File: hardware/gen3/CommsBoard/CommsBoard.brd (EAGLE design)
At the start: 140 x 100 mm, 41 parts, among them U1 ATMEGA165PV-8AU

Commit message: hooked up comms to spare header. added breakbeam sensor
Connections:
- new net SPARE1: SPARE_HEADER.1, U1.25
- new net SPARE2: SPARE_HEADER.2, U1.26
- new net SPARE3: SPARE_HEADER.3, U1.27
- new net SPARE4: SPARE_HEADER.4, U1.28
- new net SPARE5: SPARE_HEADER.5, U1.29
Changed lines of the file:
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@@
 <wire x1="81.28" y1="31.115" x2="81" y2="31" width="0.254" layer="1"/>
+</signal>
+<signal name="SPARE1">
+<contactref element="U1" pad="25"/>
+<contactref element="SPARE_HEADER" pad="1"/>
+<wire x1="94" y1="3.127" x2="77.62" y2="68.4064" width="0" layer="19" extent="1-1"/>
+</signal>
+<signal name="SPARE2">
+<contactref element="SPARE_HEADER" pad="2"/>
+<contactref element="U1" pad="26"/>
+<wire x1="96.54" y1="2.873" x2="77.62" y2="69.1938" width="0" layer="19" extent="1-1"/>
+</signal>
+<signal name="SPARE3">
+<contactref element="U1" pad="27"/>
+<contactref element="SPARE_HEADER" pad="3"/>
+<wire x1="99.08" y1="3.127" x2="77.62" y2="70.0066" width="0" layer="19" extent="1-1"/>
+</signal>
+<signal name="SPARE4">
+<contactref element="SPARE_HEADER" pad="4"/>
+<contactref element="U1" pad="28"/>
+<wire x1="101.62" y1="2.873" x2="77.62" y2="70.794" width="0" layer="19" extent="1-1"/>
+</signal>
+<signal name="SPARE5">
+<contactref element="U1" pad="29"/>
+<contactref element="SPARE_HEADER" pad="5"/>
+<wire x1="104.16" y1="3.127" x2="77.62" y2="71.6068" width="0" layer="19" extent="1-1"/>
 </signal>
 </signals>

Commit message: added comments
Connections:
- new net SS_E4: SPI_HEADER.9, U1.56
- new net SS_E5: SPI_HEADER.10, U1.55
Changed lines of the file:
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@@
 <wire x1="104.16" y1="3.127" x2="77.62" y2="71.6068" width="0" layer="19" extent="1-1"/>
+</signal>
+<signal name="SS_E4">
+<contactref element="SPI_HEADER" pad="9"/>
+<contactref element="U1" pad="56"/>
+<wire x1="62.38" y1="68.4064" x2="114.32" y2="97.127" width="0" layer="19" extent="1-1"/>
+</signal>
+<signal name="SS_E5">
+<contactref element="SPI_HEADER" pad="10"/>
+<contactref element="U1" pad="55"/>
+<wire x1="62.38" y1="69.1938" x2="116.86" y2="96.873" width="0" layer="19" extent="1-1"/>
 </signal>
 </signals>

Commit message: some decoupling for power lines
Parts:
- added C5, C6: .1uF, SparkFun-Capacitors:0805
- R2, R3, R4: value 10k -> 4.7k
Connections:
- net 3.3V: now also C6.1
- net 5V: now also C5.1
- net GND: now also C5.2, C6.2
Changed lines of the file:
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@@
 <layers>
 <layer number="1" name="Top" color="4" fill="1" visible="yes" active="yes"/>
+<layer number="2" name="Route2" color="1" fill="3" visible="no" active="no"/>
+<layer number="3" name="Route3" color="4" fill="3" visible="no" active="no"/>
+<layer number="14" name="Route14" color="1" fill="6" visible="no" active="no"/>
+<layer number="15" name="Route15" color="4" fill="6" visible="no" active="no"/>
 <layer number="16" name="Bottom" color="1" fill="1" visible="yes" active="yes"/>
 <layer number="17" name="Pads" color="2" fill="1" visible="yes" active="yes"/>
@@
 <layer number="223" name="223bmp" color="24" fill="1" visible="no" active="no"/>
 <layer number="224" name="224bmp" color="25" fill="1" visible="no" active="no"/>
+<layer number="225" name="225bmp" color="7" fill="1" visible="yes" active="yes"/>
+<layer number="226" name="226bmp" color="7" fill="1" visible="yes" active="yes"/>
+<layer number="227" name="227bmp" color="7" fill="1" visible="yes" active="yes"/>
+<layer number="228" name="228bmp" color="7" fill="1" visible="yes" active="yes"/>
+<layer number="229" name="229bmp" color="7" fill="1" visible="yes" active="yes"/>
+<layer number="230" name="230bmp" color="7" fill="1" visible="yes" active="yes"/>
+<layer number="231" name="231bmp" color="7" fill="1" visible="yes" active="yes"/>
 <layer number="248" name="Housing" color="7" fill="1" visible="yes" active="yes"/>
 <layer number="249" name="Edge" color="7" fill="1" visible="yes" active="yes"/>
@@
 <element name="C2" library="SparkFun-Capacitors" package="0805" value=".1uF" x="56" y="63" rot="R270"/>
 <element name="R1" library="SparkFun-Passives" package="0805" value="10k" x="56" y="59" rot="R270"/>
-<element name="R2" library="SparkFun-Passives" package="0805" value="10k" x="94" y="92" rot="R90"/>
-<element name="R3" library="SparkFun-Passives" package="0805" value="10k" x="97" y="88" rot="R90"/>
-<element name="R4" library="SparkFun-Passives" package="0805" value="10k" x="100" y="92" rot="R90"/>
+<element name="R2" library="SparkFun-Passives" package="0805" value="4.7k" x="94" y="92" rot="R90"/>
+<element name="R3" library="SparkFun-Passives" package="0805" value="4.7k" x="97" y="88" rot="R90"/>
+<element name="R4" library="SparkFun-Passives" package="0805" value="4.7k" x="100" y="92" rot="R90"/>
 <element name="FRAME2" library="SparkFun-Aesthetics" package="CREATIVE_COMMONS" value="FRAME-LETTER" x="88.95" y="-14.47"/>
 <element name="ROBID" library="SparkFun-Electromechanical" package="4-POS-DIP-SMD" value="4-POS-DIP" x="10" y="43" rot="R270">
@@
 </element>
 <element name="JP1" library="SparkFun-Connectors" package="AVR_ICSP" value="M05X2PTH" x="71" y="5" rot="R90"/>
+<element name="C5" library="SparkFun-Capacitors" package="0805" value=".1uF" x="-2" y="-27"/>
+<element name="C6" library="SparkFun-Capacitors" package="0805" value=".1uF" x="-5" y="-27"/>
 </elements>
 <signals>
@@
 <vertex x="1" y="79.4"/>
 </polygon>
+<contactref element="C6" pad="2"/>
+<contactref element="C5" pad="2"/>
+<wire x1="-1.1" y1="-27" x2="59.055" y2="15.5575" width="0" layer="19" extent="1-16"/>
+<wire x1="-4.1" y1="-27" x2="-1.1" y2="-27" width="0" layer="19" extent="1-1"/>
 </signal>
 <signal name="3.3V">
@@
 <wire x1="5.715" y1="73.025" x2="5.555" y2="72.81" width="0.254" layer="1"/>
 <via x="6.985" y="74.295" extent="1-16" drill="0.6096"/>
+<contactref element="C6" pad="1"/>
+<wire x1="-5.9" y1="-27" x2="5.715" y2="39.0525" width="0" layer="19" extent="1-1"/>
 </signal>
 <signal name="FILT">
@@
 <wire x1="33.3375" y1="97.155" x2="33.16" y2="97.127" width="0.254" layer="1"/>
 <wire x1="35.56" y1="97.155" x2="35.7" y2="96.873" width="0.254" layer="1"/>
+<contactref element="C5" pad="1"/>
+<wire x1="-2.9" y1="-27" x2="33.16" y2="97.127" width="0" layer="19" extent="1-1"/>
 </signal>
 <signal name="12VGND">

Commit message: added tmp sensor
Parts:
- added U$2: MCP9700SMD, SparkFun-Sensors:SOT23-3
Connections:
- new net TSENSE: U$2.2, U1.54
- net 3.3V: now also U$2.1
- net GND: now also U$2.3
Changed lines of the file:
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@@
 <element name="C5" library="SparkFun-Capacitors" package="0805" value=".1uF" x="-2" y="-27"/>
 <element name="C6" library="SparkFun-Capacitors" package="0805" value=".1uF" x="-5" y="-27"/>
+<element name="U$2" library="SparkFun-Sensors" package="SOT23-3" value="MCP9700SMD" x="-9" y="-27">
+<attribute name="PROD_ID" value="IC-08917" x="-9" y="-27" size="1.778" layer="27" display="off"/>
+</element>
 </elements>
 <signals>
@@
 <contactref element="C6" pad="2"/>
 <contactref element="C5" pad="2"/>
+<contactref element="U$2" pad="3"/>
 <wire x1="-1.1" y1="-27" x2="59.055" y2="15.5575" width="0" layer="19" extent="1-16"/>
 <wire x1="-4.1" y1="-27" x2="-1.1" y2="-27" width="0" layer="19" extent="1-1"/>
+<wire x1="-9" y1="-25.9" x2="-4.1" y2="-27" width="0" layer="19" extent="1-1"/>
 </signal>
 <signal name="3.3V">
@@
 <via x="6.985" y="74.295" extent="1-16" drill="0.6096"/>
 <contactref element="C6" pad="1"/>
+<contactref element="U$2" pad="1"/>
 <wire x1="-5.9" y1="-27" x2="5.715" y2="39.0525" width="0" layer="19" extent="1-1"/>
+<wire x1="-9.95" y1="-28" x2="-5.9" y2="-27" width="0" layer="19" extent="1-1"/>
 </signal>
 <signal name="FILT">
@@
 <wire x1="62.38" y1="69.1938" x2="116.86" y2="96.873" width="0" layer="19" extent="1-1"/>
 </signal>
+<signal name="TSENSE">
+<contactref element="U$2" pad="2"/>
+<contactref element="U1" pad="54"/>
+<wire x1="-8.05" y1="-28" x2="62.38" y2="70.0066" width="0" layer="19" extent="1-1"/>
+</signal>
 </signals>

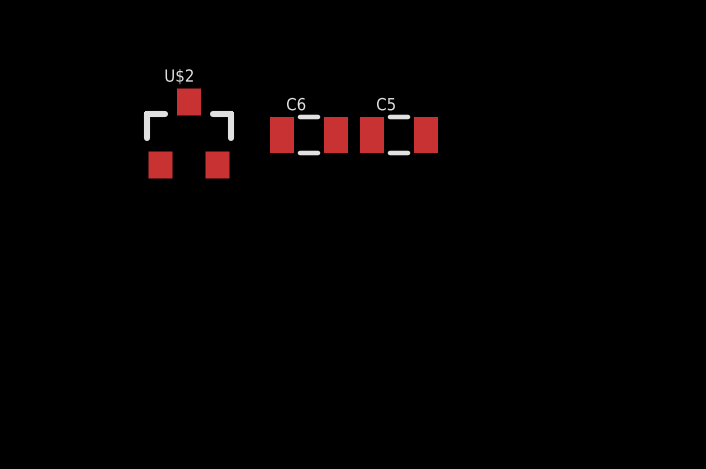
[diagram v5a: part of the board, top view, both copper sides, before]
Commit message: Added reset button to comms
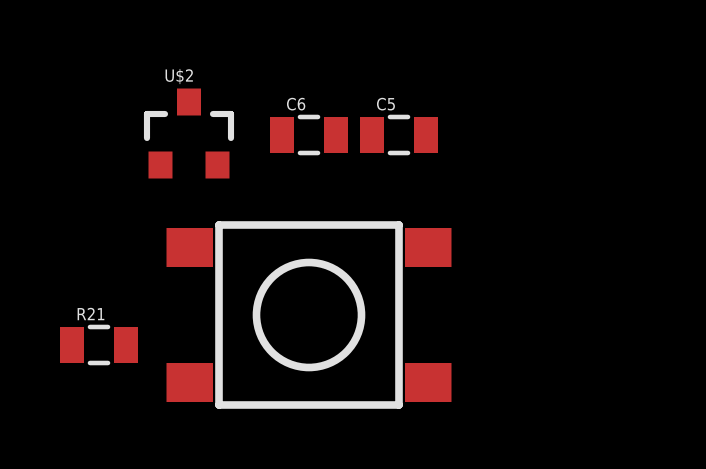
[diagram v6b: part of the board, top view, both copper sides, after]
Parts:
- added R21: 10k, SparkFun-Passives:0805
- added S1: SWITCH-MOMENTARY-2SMD-4, SparkFun-Electromechanical:TACTILE_SWITCH_TALL
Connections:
- net 3.3V: now also R21.2
- net GND: now also S1.B2
- net RESET: now also R21.1, S1.A2
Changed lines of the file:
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@@
 <?xml version="1.0" encoding="utf-8"?>
 <!DOCTYPE eagle SYSTEM "eagle.dtd">
-<eagle version="6.4">
+<eagle version="7.2.0">
 <drawing>
 <settings>
@@
 <pass name="Default">
 <param name="RoutingGrid" value="12.5mil"/>
+<param name="AutoGrid" value="1"/>
+<param name="Efforts" value="0"/>
+<param name="TopRouterVariant" value="1"/>
 <param name="tpViaShape" value="round"/>
 <param name="PrefDir.1" value="*"/>
@@
 <attribute name="PROD_ID" value="IC-08917" x="-9" y="-27" size="1.778" layer="27" display="off"/>
 </element>
+<element name="S1" library="SparkFun-Electromechanical" package="TACTILE_SWITCH_TALL" value="SWITCH-MOMENTARY-2SMD-4" x="-5" y="-33">
+<attribute name="PROD_ID" value="SWCH-11966" x="-5" y="-33" size="1.778" layer="27" display="off"/>
+</element>
+<element name="R21" library="SparkFun-Passives" package="0805" value="10k" x="-12" y="-34"/>
 </elements>
 <signals>
@@
 <contactref element="C5" pad="2"/>
 <contactref element="U$2" pad="3"/>
+<contactref element="S1" pad="B2"/>
 <wire x1="-1.1" y1="-27" x2="59.055" y2="15.5575" width="0" layer="19" extent="1-16"/>
 <wire x1="-4.1" y1="-27" x2="-1.1" y2="-27" width="0" layer="19" extent="1-1"/>
+<wire x1="-1.025" y1="-30.75" x2="-1.1" y2="-27" width="0" layer="19" extent="1-1"/>
 <wire x1="-9" y1="-25.9" x2="-4.1" y2="-27" width="0" layer="19" extent="1-1"/>
 </signal>
@@
 <contactref element="C6" pad="1"/>
 <contactref element="U$2" pad="1"/>
+<contactref element="R21" pad="2"/>
 <wire x1="-5.9" y1="-27" x2="5.715" y2="39.0525" width="0" layer="19" extent="1-1"/>
 <wire x1="-9.95" y1="-28" x2="-5.9" y2="-27" width="0" layer="19" extent="1-1"/>
+<wire x1="-11.1" y1="-34" x2="-9.95" y2="-28" width="0" layer="19" extent="1-1"/>
 </signal>
 <signal name="FILT">
@@
 <wire x1="77.7875" y1="64.4525" x2="77.62" y2="64.3932" width="0.254" layer="1"/>
 <wire x1="71.12" y1="3.4925" x2="71" y2="3.73" width="0.254" layer="1"/>
+<contactref element="S1" pad="A2"/>
+<contactref element="R21" pad="1"/>
+<wire x1="-1.025" y1="-35.25" x2="71.12" y2="3.4925" width="0" layer="19" extent="1-1"/>
+<wire x1="-12.9" y1="-34" x2="-1.025" y2="-35.25" width="0" layer="19" extent="1-1"/>
 </signal>
 <signal name="12V">

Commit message: Added IMU header to comms board
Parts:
- added M5LOCK: IMU_HEADER, SparkFun-Connectors:1X05_LOCK
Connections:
- new net INT: M5LOCK.1, U1.5
- new net SCL: M5LOCK.2, U1.6
- new net SDA: M5LOCK.3, U1.7
- net 3.3V: now also M5LOCK.5
- net CTS: now also U1.9; no longer U1.6
- net GND: now also M5LOCK.4
- net RTS: now also U1.8; no longer U1.5
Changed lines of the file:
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@@
 </element>
 <element name="R21" library="SparkFun-Passives" package="0805" value="10k" x="-12" y="-34"/>
+<element name="M5LOCK" library="SparkFun-Connectors" package="1X05_LOCK" value="IMU_HEADER" x="-11" y="-40"/>
 </elements>
 <signals>
@@
 <contactref element="U$2" pad="3"/>
 <contactref element="S1" pad="B2"/>
+<contactref element="M5LOCK" pad="4"/>
 <wire x1="-1.1" y1="-27" x2="59.055" y2="15.5575" width="0" layer="19" extent="1-16"/>
 <wire x1="-4.1" y1="-27" x2="-1.1" y2="-27" width="0" layer="19" extent="1-1"/>
 <wire x1="-1.025" y1="-30.75" x2="-1.1" y2="-27" width="0" layer="19" extent="1-1"/>
 <wire x1="-9" y1="-25.9" x2="-4.1" y2="-27" width="0" layer="19" extent="1-1"/>
+<wire x1="-3.38" y1="-40.127" x2="-1.025" y2="-30.75" width="0" layer="19" extent="1-1"/>
 </signal>
 <signal name="3.3V">
@@
 <contactref element="U$2" pad="1"/>
 <contactref element="R21" pad="2"/>
+<contactref element="M5LOCK" pad="5"/>
 <wire x1="-5.9" y1="-27" x2="5.715" y2="39.0525" width="0" layer="19" extent="1-1"/>
 <wire x1="-9.95" y1="-28" x2="-5.9" y2="-27" width="0" layer="19" extent="1-1"/>
 <wire x1="-11.1" y1="-34" x2="-9.95" y2="-28" width="0" layer="19" extent="1-1"/>
+<wire x1="-0.84" y1="-39.873" x2="-11.1" y2="-34" width="0" layer="19" extent="1-1"/>
 </signal>
 <signal name="FILT">
@@
 <signal name="RTS">
 <contactref element="U$1" pad="16"/>
-<contactref element="U1" pad="5"/>
 <wire x1="67.31" y1="52.705" x2="67.31" y2="60.325" width="0.254" layer="1"/>
 <wire x1="80.9625" y1="39.0525" x2="67.31" y2="52.705" width="0.254" layer="1"/>
-<wire x1="67.31" y1="60.325" x2="67.206" y2="60.38" width="0.254" layer="1"/>
 <wire x1="80.9625" y1="39.0525" x2="81" y2="39" width="0.254" layer="1"/>
+<contactref element="U1" pad="8"/>
+<wire x1="67.31" y1="60.325" x2="69.5936" y2="60.38" width="0" layer="19" extent="1-1"/>
 </signal>
 <signal name="CTS">
 <contactref element="U$1" pad="12"/>
-<contactref element="U1" pad="6"/>
 <wire x1="67.945" y1="59.69" x2="67.945" y2="60.325" width="0.254" layer="1"/>
 <wire x1="79.375" y1="48.26" x2="67.945" y2="59.69" width="0.254" layer="1"/>
@@
 <wire x1="82.2325" y1="32.0675" x2="82.2325" y2="47.625" width="0.254" layer="1"/>
 <wire x1="81.28" y1="31.115" x2="82.2325" y2="32.0675" width="0.254" layer="1"/>
-<wire x1="67.945" y1="60.325" x2="67.9934" y2="60.38" width="0.254" layer="1"/>
 <wire x1="81.28" y1="31.115" x2="81" y2="31" width="0.254" layer="1"/>
+<contactref element="U1" pad="9"/>
+<wire x1="67.945" y1="60.325" x2="70.4064" y2="60.38" width="0" layer="19" extent="1-1"/>
 </signal>
 <signal name="SPARE1">
@@
 <wire x1="-8.05" y1="-28" x2="62.38" y2="70.0066" width="0" layer="19" extent="1-1"/>
 </signal>
+<signal name="INT">
+<contactref element="U1" pad="5"/>
+<contactref element="M5LOCK" pad="1"/>
+<wire x1="-11" y1="-39.873" x2="67.206" y2="60.38" width="0" layer="19" extent="1-1"/>
+</signal>
+<signal name="SCL">
+<contactref element="U1" pad="6"/>
+<contactref element="M5LOCK" pad="2"/>
+<wire x1="-8.46" y1="-40.127" x2="67.9934" y2="60.38" width="0" layer="19" extent="1-1"/>
+</signal>
+<signal name="SDA">
+<contactref element="U1" pad="7"/>
+<contactref element="M5LOCK" pad="3"/>
+<wire x1="-5.92" y1="-39.873" x2="68.8062" y2="60.38" width="0" layer="19" extent="1-1"/>
+</signal>
 </signals>

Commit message: Added IMU package
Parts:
- removed M5LOCK: IMU_HEADER, SparkFun-Connectors:1X05_LOCK
- added IMU: MPU6050IMUMPU, gen3:MPU-6050IMU
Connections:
- net 3.3V: now also IMU.VCC; no longer M5LOCK.5
- net GND: now also IMU.GND; no longer M5LOCK.4
- net INT: now also IMU.INT; no longer M5LOCK.1
- net SCL: now also IMU.SCL; no longer M5LOCK.2
- net SDA: now also IMU.SDA; no longer M5LOCK.3
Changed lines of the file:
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@@
 </element>
 <element name="R21" library="SparkFun-Passives" package="0805" value="10k" x="-12" y="-34"/>
-<element name="M5LOCK" library="SparkFun-Connectors" package="1X05_LOCK" value="IMU_HEADER" x="-11" y="-40"/>
+<element name="IMU" library="gen3" package="MPU-6050IMU" value="MPU6050IMUMPU" x="-27" y="-33"/>
 </elements>
 <signals>
@@
 <contactref element="U$2" pad="3"/>
 <contactref element="S1" pad="B2"/>
-<contactref element="M5LOCK" pad="4"/>
+<contactref element="IMU" pad="GND"/>
 <wire x1="-1.1" y1="-27" x2="59.055" y2="15.5575" width="0" layer="19" extent="1-16"/>
 <wire x1="-4.1" y1="-27" x2="-1.1" y2="-27" width="0" layer="19" extent="1-1"/>
 <wire x1="-1.025" y1="-30.75" x2="-1.1" y2="-27" width="0" layer="19" extent="1-1"/>
 <wire x1="-9" y1="-25.9" x2="-4.1" y2="-27" width="0" layer="19" extent="1-1"/>
-<wire x1="-3.38" y1="-40.127" x2="-1.025" y2="-30.75" width="0" layer="19" extent="1-1"/>
+<wire x1="-27" y1="-30.46" x2="-9" y2="-25.9" width="0" layer="19" extent="1-1"/>
 </signal>
 <signal name="3.3V">
@@
 <contactref element="U$2" pad="1"/>
 <contactref element="R21" pad="2"/>
-<contactref element="M5LOCK" pad="5"/>
-<wire x1="-5.9" y1="-27" x2="5.715" y2="39.0525" width="0" layer="19" extent="1-1"/>
-<wire x1="-9.95" y1="-28" x2="-5.9" y2="-27" width="0" layer="19" extent="1-1"/>
-<wire x1="-11.1" y1="-34" x2="-9.95" y2="-28" width="0" layer="19" extent="1-1"/>
-<wire x1="-0.84" y1="-39.873" x2="-11.1" y2="-34" width="0" layer="19" extent="1-1"/>
+<contactref element="IMU" pad="VCC"/>
+<wire x1="-11.1" y1="-34" x2="-27" y2="-27.92" width="0" layer="19" extent="1-1"/>
+<wire x1="-9.95" y1="-28" x2="-11.1" y2="-34" width="0" layer="19" extent="1-1"/>
+<wire x1="-5.9" y1="-27" x2="-9.95" y2="-28" width="0" layer="19" extent="1-1"/>
+<wire x1="5.715" y1="39.0525" x2="-5.9" y2="-27" width="0" layer="19" extent="1-1"/>
 </signal>
 <signal name="FILT">
@@
 <signal name="INT">
 <contactref element="U1" pad="5"/>
-<contactref element="M5LOCK" pad="1"/>
-<wire x1="-11" y1="-39.873" x2="67.206" y2="60.38" width="0" layer="19" extent="1-1"/>
+<contactref element="IMU" pad="INT"/>
+<wire x1="-27" y1="-38.08" x2="67.206" y2="60.38" width="0" layer="19" extent="1-1"/>
 </signal>
 <signal name="SCL">
 <contactref element="U1" pad="6"/>
-<contactref element="M5LOCK" pad="2"/>
-<wire x1="-8.46" y1="-40.127" x2="67.9934" y2="60.38" width="0" layer="19" extent="1-1"/>
+<contactref element="IMU" pad="SCL"/>
+<wire x1="-27" y1="-35.54" x2="67.9934" y2="60.38" width="0" layer="19" extent="1-1"/>
 </signal>
 <signal name="SDA">
 <contactref element="U1" pad="7"/>
-<contactref element="M5LOCK" pad="3"/>
-<wire x1="-5.92" y1="-39.873" x2="68.8062" y2="60.38" width="0" layer="19" extent="1-1"/>
+<contactref element="IMU" pad="SDA"/>
+<wire x1="-27" y1="-33" x2="68.8062" y2="60.38" width="0" layer="19" extent="1-1"/>
 </signal>
 </signals>
